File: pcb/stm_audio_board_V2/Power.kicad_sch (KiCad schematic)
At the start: 42 parts, among them U10 TL072, U2 AMS1117-3.3, U4 OP275, U5 AMS1117-3.3, U7 OP275, U8 AMS1117-5.0, U9 L7809

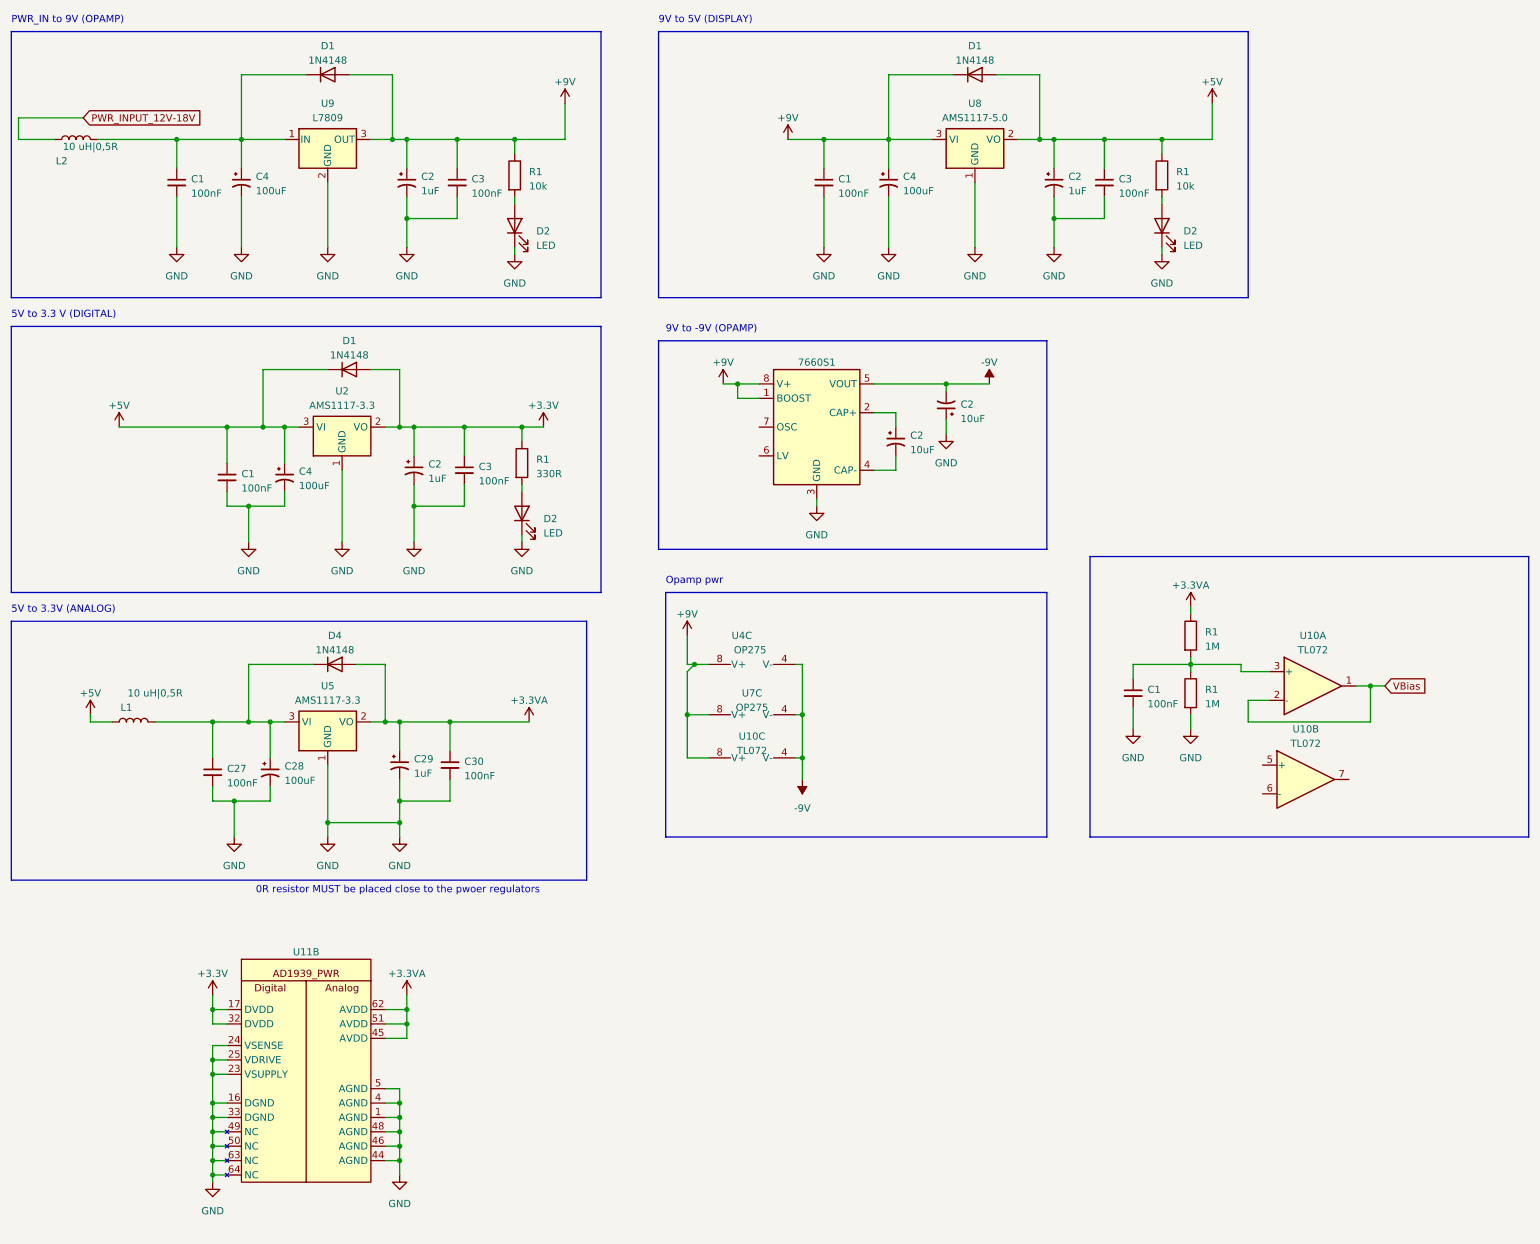
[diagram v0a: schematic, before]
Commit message: input and output stage reworked in sim and in schematic, power filtering is changed, further calculations needed
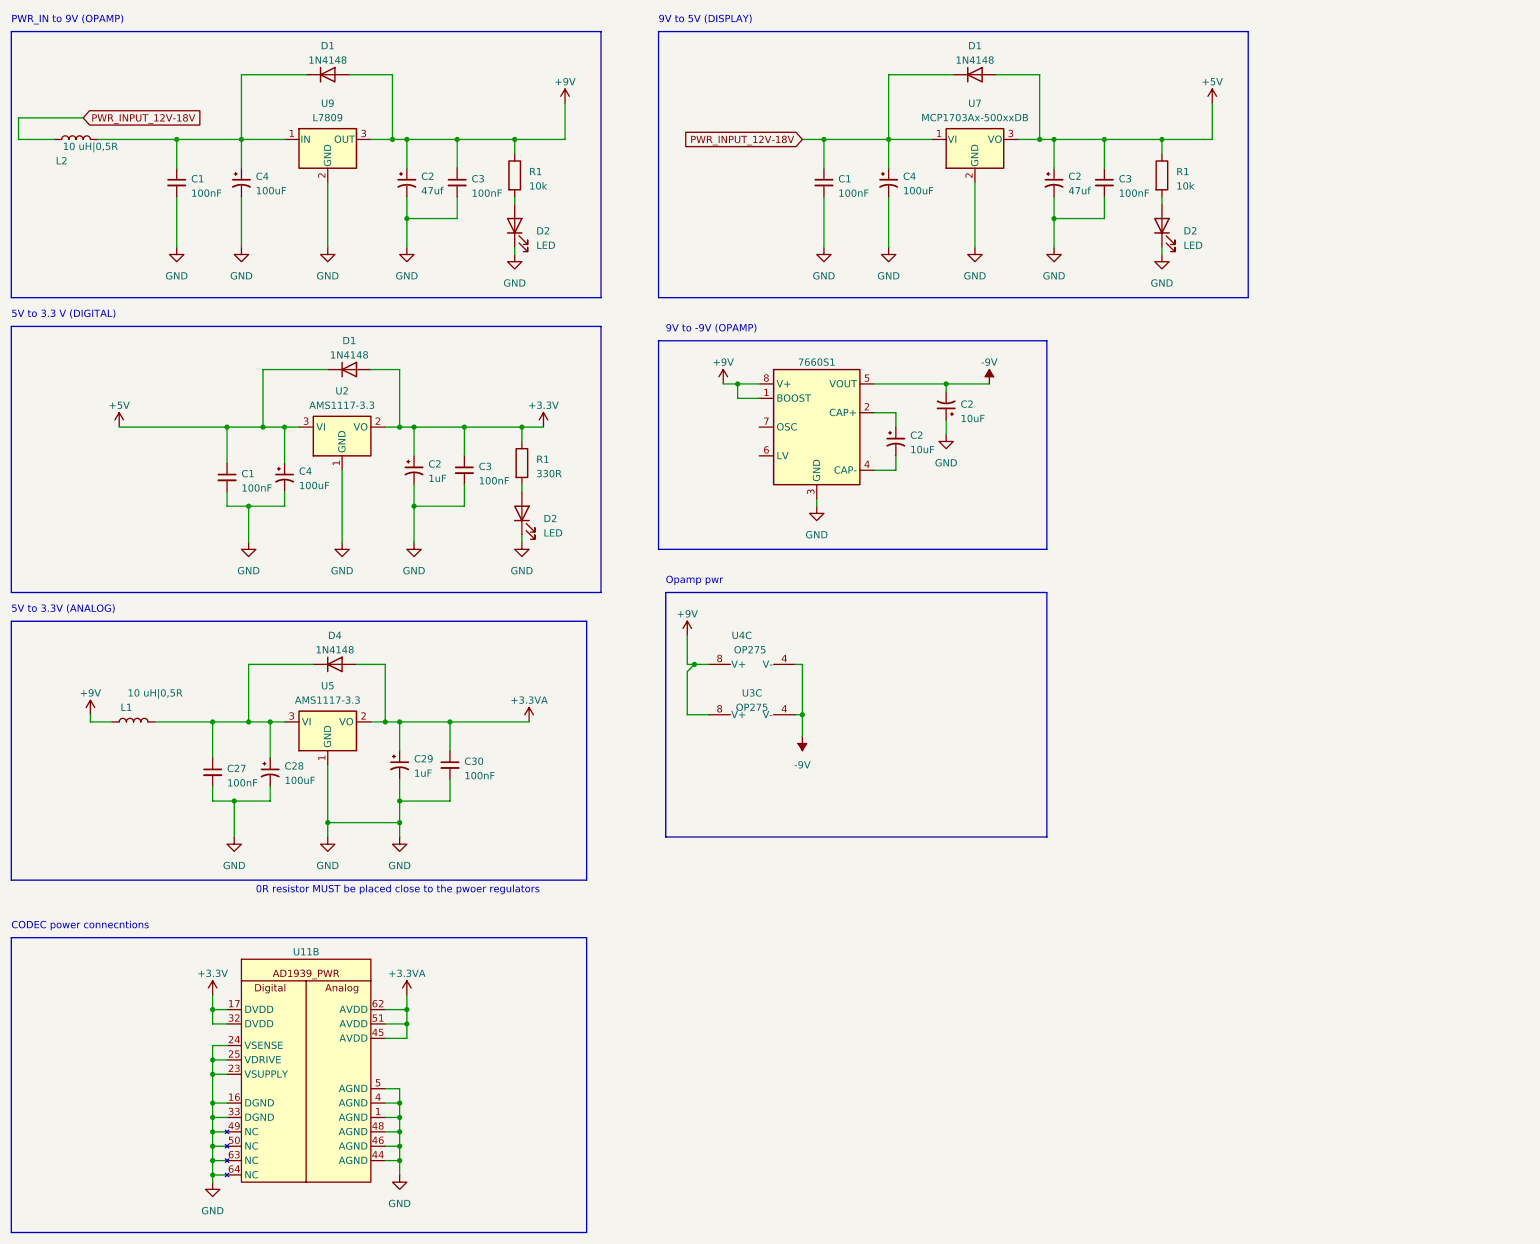
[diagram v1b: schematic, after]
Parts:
- removed C1: 100nF, Capacitor_SMD:C_0603_1608Metric_Pad1.08x0.95mm_HandSolder, symbol Device:C_Small
- removed R1 (x2): 1M, Resistor_SMD:R_0805_2012Metric_Pad1.20x1.40mm_HandSolder, symbol Device:R
- removed U10: TL072, symbol Amplifier_Operational:TL072
- removed U7: OP275, Package_SO:SSOP-8_3.9x5.05mm_P1.27mm, symbol Amplifier_Operational:OP275
- removed U8: AMS1117-5.0, Package_TO_SOT_SMD:SOT-223-3_TabPin2, symbol Regulator_Linear:AMS1117-5.0
- added U3: OP275, symbol Amplifier_Operational:OP275
- added U7: MCP1703Ax-500xxDB, Package_TO_SOT_SMD:SOT-223-3_TabPin2, symbol Regulator_Linear:MCP1703Ax-500xxDB
- C2: value 1uF -> 47uf
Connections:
- net +5V: now also U7.3 (VO); no longer L1.1
- net +9V: now also L1.1, U3.8 (V+); no longer C1.1, C4.1, D1.1 (K)
- net -9V: now also U3.4 (V-)
- net GND: now also U7.2 (GND)
- net PWR_INPUT_12V-18V: now also C1.1, C4.1, D1.1 (K), U7.1 (VI)
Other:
- note added: "CODEC power connecntions"

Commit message: Update ad1939_dif.log, ad1939_dif.op.raw, and 6 more files...
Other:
- note added: "18V to 5V"
- note added: "9V to 3.3V (ANALOG)"
- note removed: "5V to 3.3V (ANALOG)"
- note removed: "9V to 5V (DISPLAY)"
- moved on the sheet: 7660S1, C1, C2, C27, C28, C29, C3, C30, C4, D1, D2, D4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

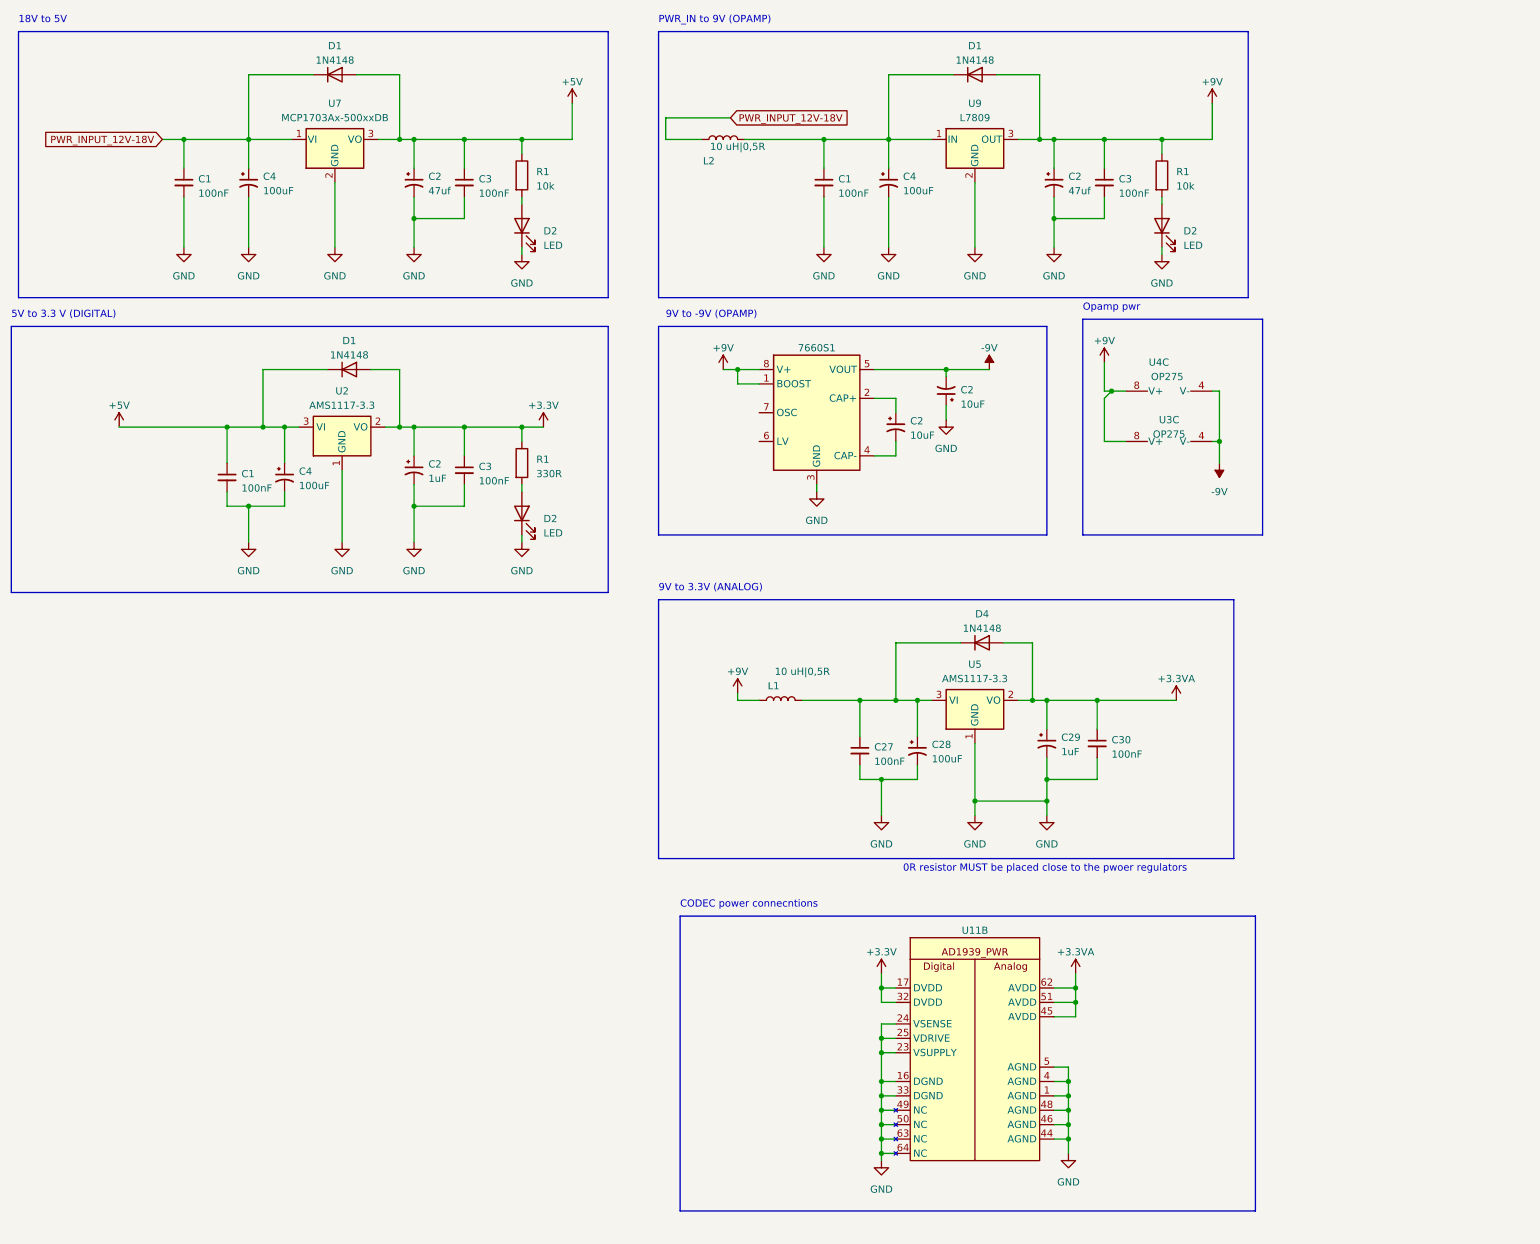
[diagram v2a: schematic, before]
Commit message: PCB design started INPUT and OUTPUT stage done, codec placed
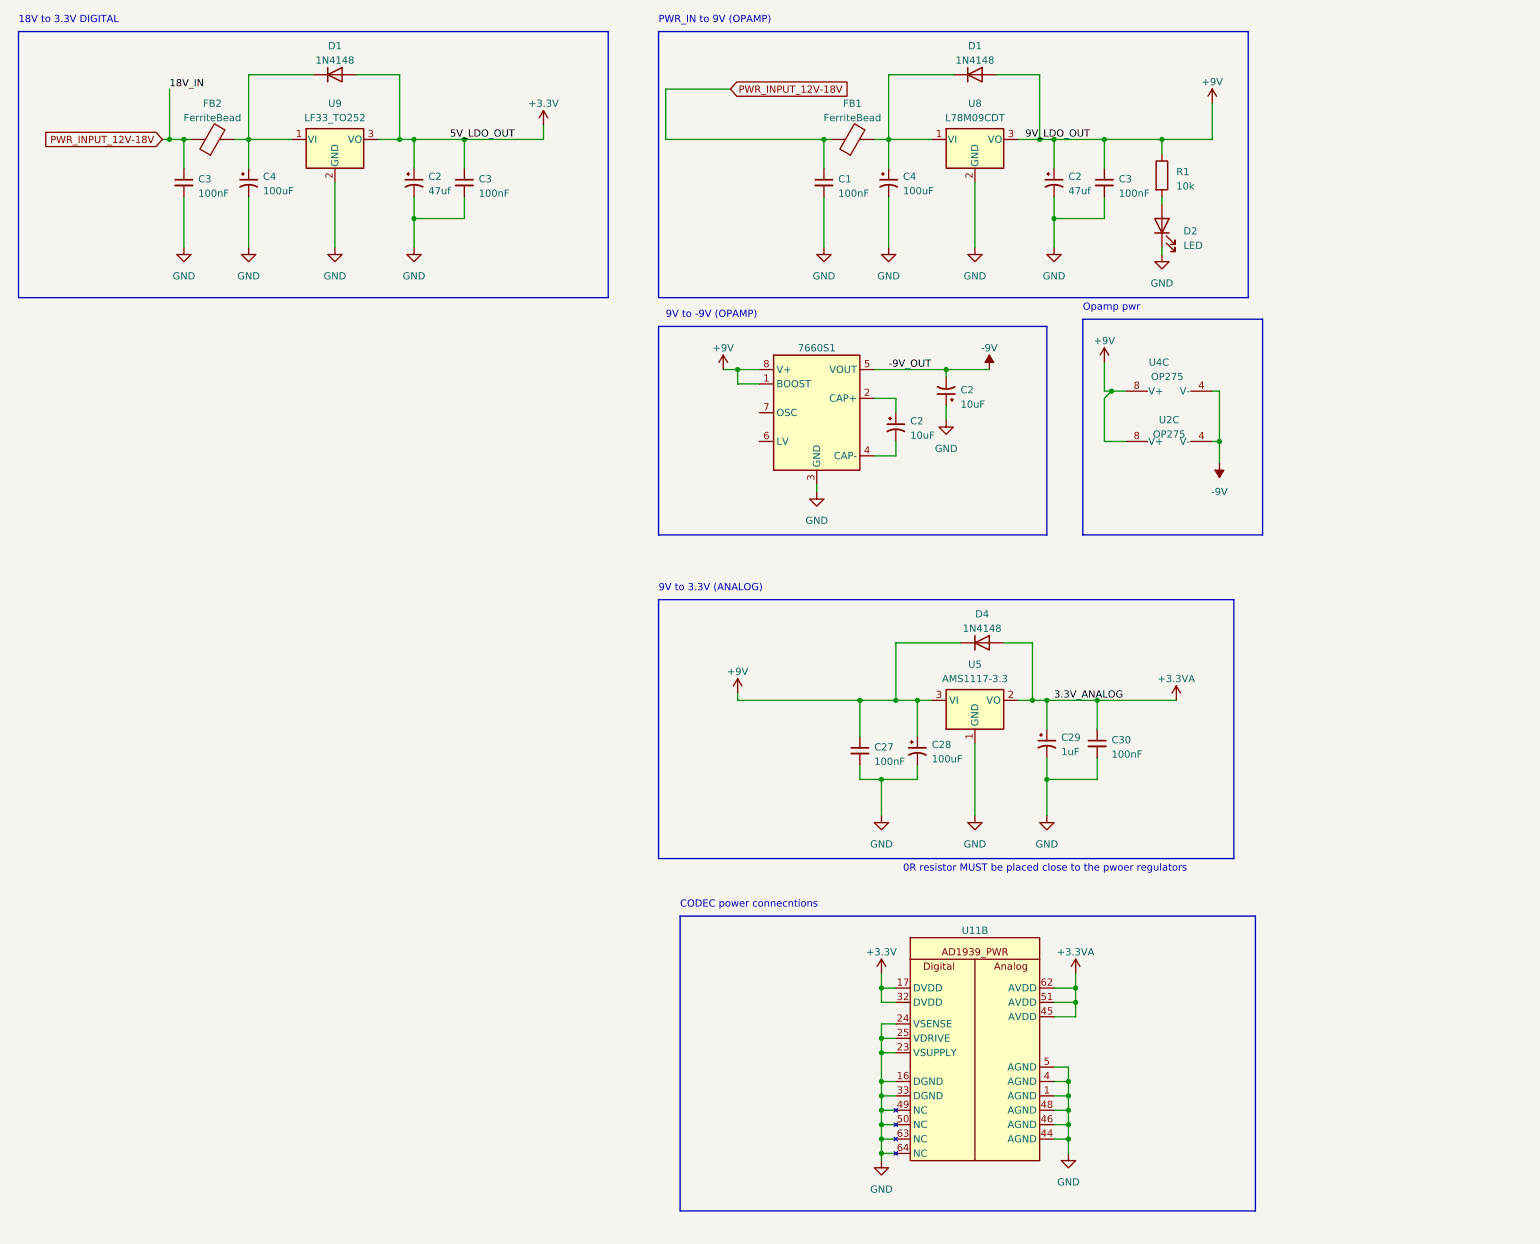
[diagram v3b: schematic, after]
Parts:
- removed C1 (x2): 100nF, Capacitor_SMD:C_0603_1608Metric_Pad1.08x0.95mm_HandSolder, symbol Device:C_Small
- removed C2: 1uF, Capacitor_THT:CP_Radial_D6.3mm_P2.50mm, symbol Device:C_Polarized_Small_US
- removed C4: 100uF, Capacitor_THT:CP_Radial_D6.3mm_P2.50mm, symbol Device:C_Polarized_Small_US
- removed D1: 1N4148, Diode_THT:D_DO-35_SOD27_P7.62mm_Horizontal, symbol Diode:1N4148
- removed D2 (x2): LED, LED_SMD:LED_SK6805_PLCC4_2.4x2.7mm_P1.3mm, symbol Device:LED
- removed L1, L2: 10 uH|0,5R, Inductor_THT:L_Axial_L9.5mm_D4.0mm_P12.70mm_Horizontal_Fastron_SMCC, symbol Device:L
- removed R1: 330R, Resistor_SMD:R_0805_2012Metric_Pad1.20x1.40mm_HandSolder, symbol Device:R
- removed R1: 10k, Resistor_SMD:R_0805_2012Metric_Pad1.20x1.40mm_HandSolder, symbol Device:R
- removed U2: AMS1117-3.3, Package_TO_SOT_SMD:SOT-223-3_TabPin2, symbol Regulator_Linear:AMS1117-3.3
- removed U3: OP275, symbol Amplifier_Operational:OP275
- removed U7: MCP1703Ax-500xxDB, Package_TO_SOT_SMD:SOT-223-3_TabPin2, symbol Regulator_Linear:MCP1703Ax-500xxDB
- removed U9: L7809, Package_TO_SOT_THT:TO-220-3_Horizontal_TabDown, symbol Regulator_Linear:L7809
- added FB1, FB2: FerriteBead, Resistor_SMD:R_0603_1608Metric_Pad0.98x0.95mm_HandSolder, symbol Device:FerriteBead
- added U2: OP275, Package_SO:SSOP-8_3.9x5.05mm_P1.27mm, symbol Amplifier_Operational:OP275
- added U8: L78M09CDT, Package_TO_SOT_SMD:TO-252-2, symbol Regulator_Linear:LF90_TO252
- added U9: LF33_TO252, Package_TO_SOT_SMD:TO-252-2, symbol Regulator_Linear:LF33_TO252
- 7660S1: footprint (none) -> Package_SO:SOIC-8_3.9x4.9mm_P1.27mm
- C4: footprint Capacitor_THT:CP_Radial_D6.3mm_P2.50mm -> Capacitor_SMD:CP_Elec_6.3x7.7
- U11: footprint (none) -> Package_QFP:LQFP-64_10x10mm_P0.5mm
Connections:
- net +5V is gone; now on net +3.3V: C2.1, C3.1, D1.2 (A)
- net +3.3V: now also U9.3 (VO); no longer C3.1
- net +9V: now also C27.1, C28.1, D4.1 (K), U5.3 (VI), U2.8 (V+), U8.3 (VO)
- net -9V: now also U2.4 (V-)
- net GND: now also U8.2 (GND), U9.2 (GND)
- net PWR_INPUT_12V-18V: now also C1.1, C3.1, FB1.1, FB2.1; no longer C4.1, D1.1 (K)
- net at C4.1, D1.1 (K): now also FB1.2, U8.1 (VI); no longer C1.1
- new net: C4.1, D1.1 (K), FB2.2, U9.1 (VI)
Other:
- note added: "18V to 3.3V DIGITAL"
- note removed: "18V to 5V"
- note removed: "5V to 3.3 V (DIGITAL)"
